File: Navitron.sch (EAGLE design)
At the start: 87 parts, among them J2 DX07S016JA1R1500, Q1 ROHM_RUM002N02T2LROHM_RUM002N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, Q2 2.5A/30V, Q3 ROHM_RUM002N02T2LROHM_RUM002N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, Q4 ROHM_RUM002N02T2LROHM_RUM002N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, Q5 ROHM_RUM002N02T2LROHM_RUM002N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, T1 BC847, T2 BC847, U2 9DoF IMU, U3 MCP73831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

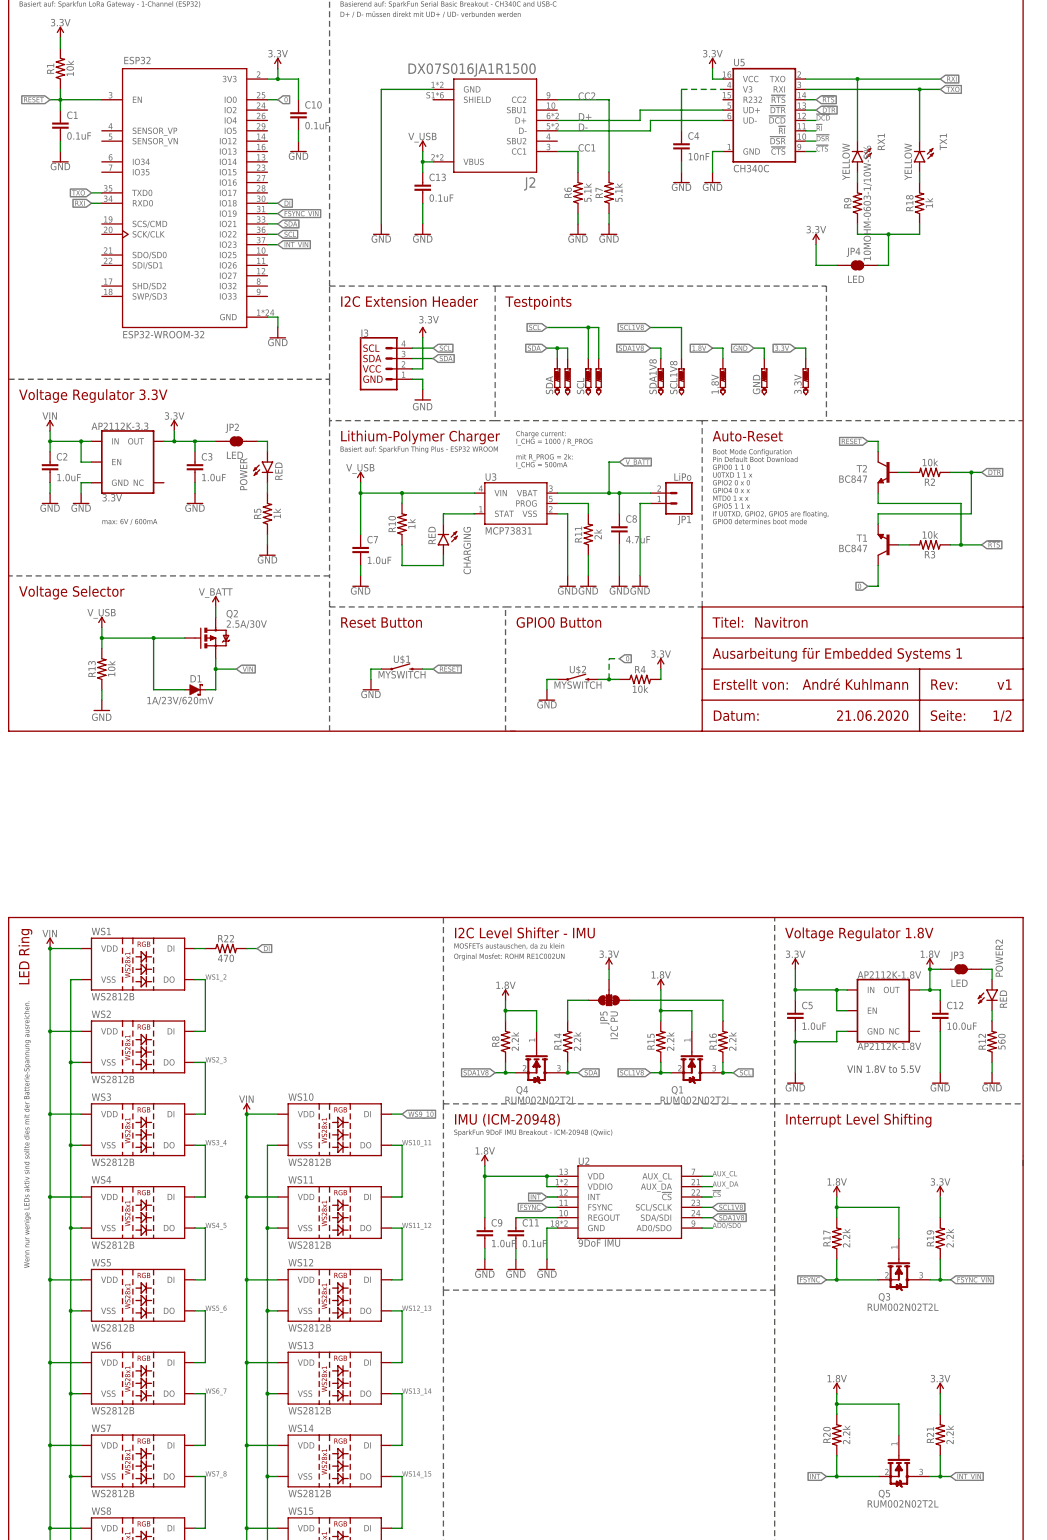
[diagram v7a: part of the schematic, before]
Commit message: Touchpads and Logos
- Added Touchpads
- Add Logos
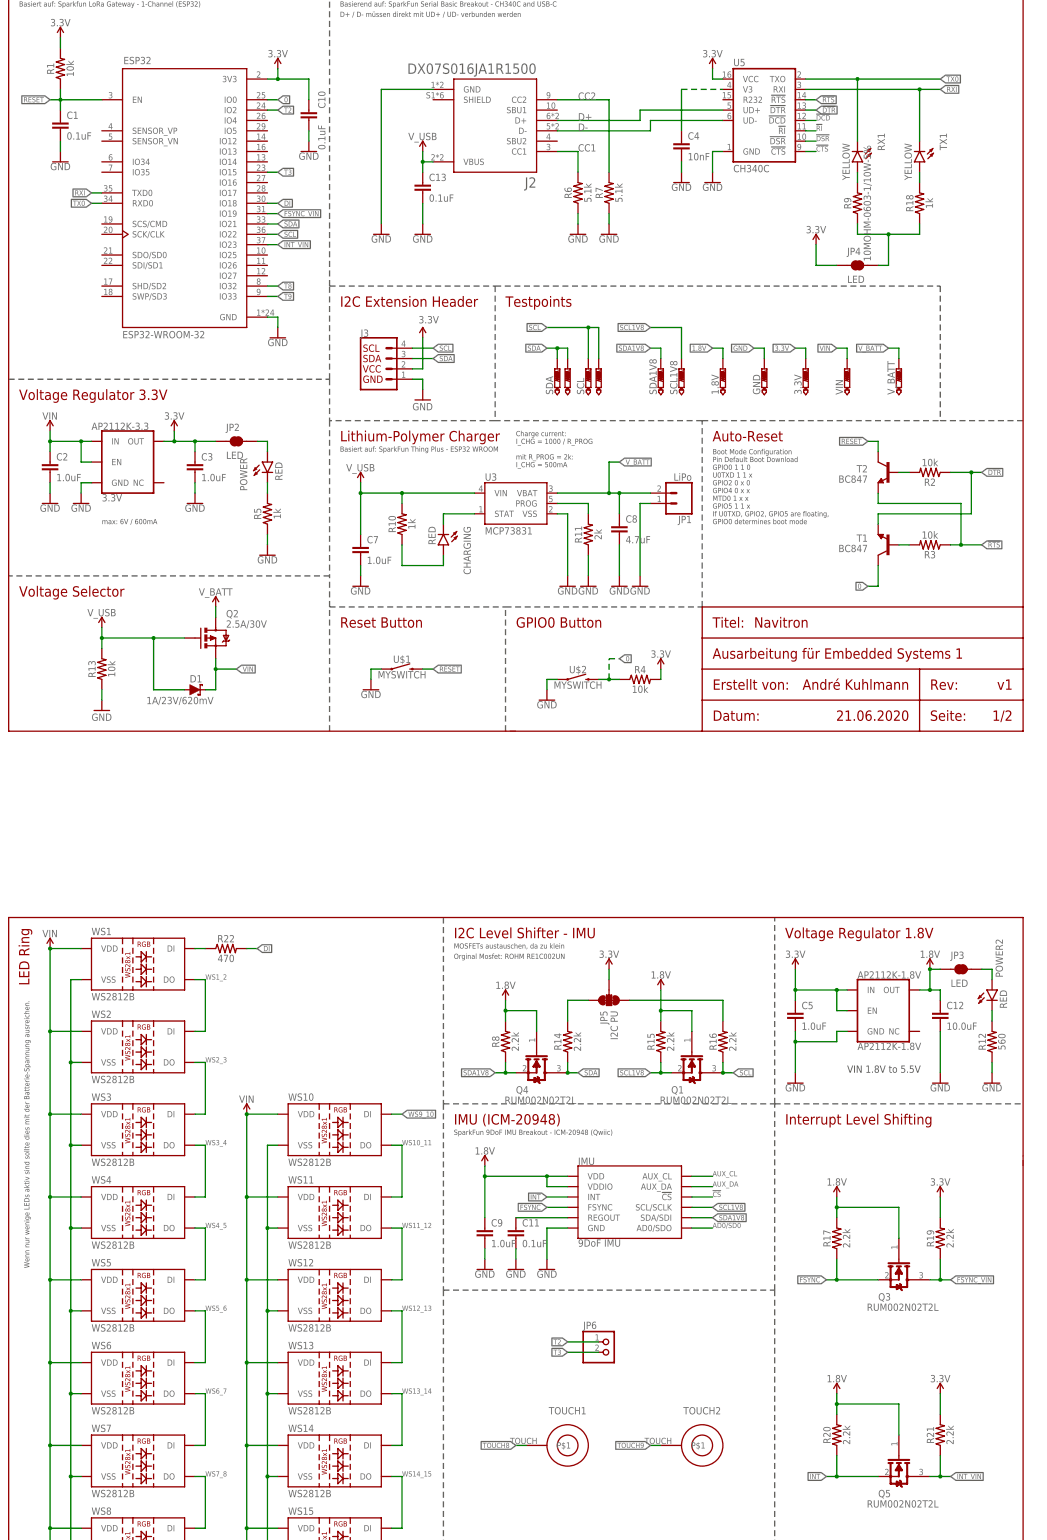
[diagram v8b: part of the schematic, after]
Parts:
- removed U2: 9DoF IMU, SparkFun-Sensors:MPU-9250
- added IMU: 9DoF IMU, SparkFun-Sensors:ICM-20948
- added JP6: (no value), pinhead:PINHD-1X2
- added TOUCH1, TOUCH2: TOUCHPAD8MM, MyLib:TOUCHPAD8MM
- added VIN, V_BATT: PTR1B1,27, testpad:PTR1B1,27
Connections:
- removed net TXO: ESP32.TXD0, TX1.C, U5.RXI
- new net T2: ESP32.IO2, JP6.1
- new net T3: ESP32.IO15, JP6.2
- new net T8: ESP32.IO32
- new net T9: ESP32.IO33
- new net TOUCH8: TOUCH1.P$1
- new net TOUCH9: TOUCH2.P$1
- new net TX0: ESP32.RXD0, RX1.C, U5.TXO
- net !CS: now also IMU.!CS; no longer U2.!CS
- net 1.8V: now also IMU.VDD, IMU.VDDIO; no longer U2.VDD, U2.VDDIO
- net AD0/SD0: now also IMU.AD0/SDO; no longer U2.AD0/SDO
- net AUX_CL: now also IMU.AUX_CL; no longer U2.AUX_CL
- net AUX_DA: now also IMU.AUX_DA; no longer U2.AUX_DA
- net FSYNC: now also IMU.FSYNC; no longer U2.FSYNC
- net GND: now also IMU.GND; no longer U2.GND
- net INT: now also IMU.INT; no longer U2.INT
- net REGOUT: now also IMU.REGOUT; no longer U2.REGOUT
- net RXI: now also ESP32.TXD0, TX1.C, U5.RXI; no longer ESP32.RXD0, RX1.C, U5.TXO
- net SCL1V8: now also IMU.SCL/SCLK; no longer U2.SCL/SCLK
- net SDA1V8: now also IMU.SDA/SDI; no longer U2.SDA/SDI
- net TO_RX_LED: now also R18.2, TX1.A; no longer R9.2, RX1.A
- net TO_TX_LED: now also R9.2, RX1.A; no longer R18.2, TX1.A
- net VIN: now also VIN.TP
- net V_BATT: now also V_BATT.TP
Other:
- moved on the sheet: C10
